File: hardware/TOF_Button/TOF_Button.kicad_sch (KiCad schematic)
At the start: 13 parts, among them J1 Potentiometer, J2 Power In Signal Out, J3 Conn_01x04_Pin, J4 Conn_01x04_Pin, U1 ADAFRUIT_QT_PY

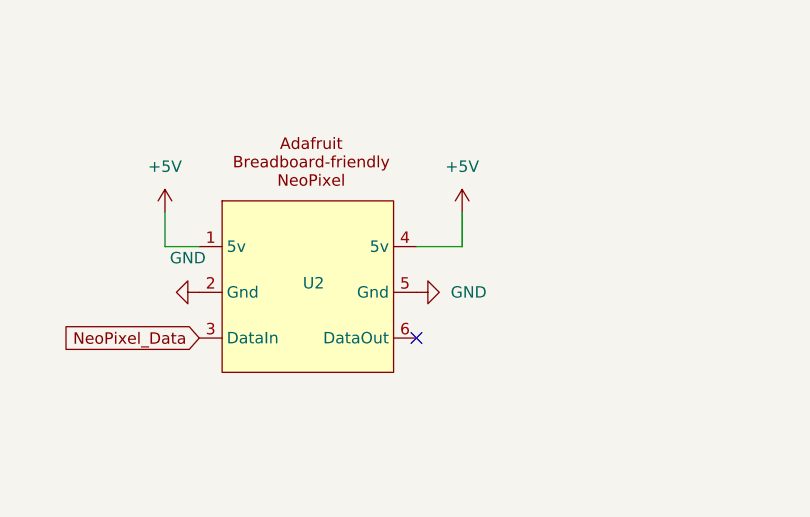
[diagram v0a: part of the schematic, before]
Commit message: fixing NeoPixel symbol for TOF Button PCB
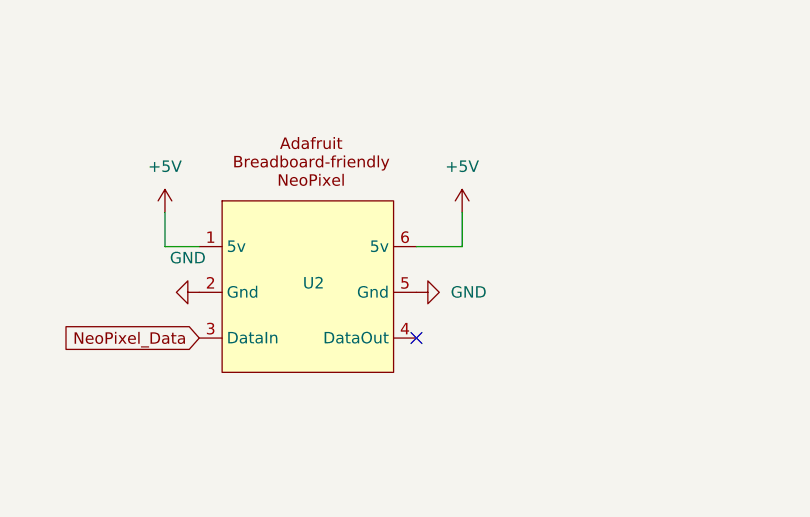
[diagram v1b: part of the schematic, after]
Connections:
- net +5V: now also U2.6 (5v); no longer U2.4 (5v)
